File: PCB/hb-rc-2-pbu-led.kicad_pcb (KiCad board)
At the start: 2 copper layers, 49.5 x 45 mm, 33 parts, among them IC1 CC1101, J1 WS2812B LED 3V3 Lvl, J10 3V3 PAD, J11 5V PAD, J12 DIN, J13 DOUT, J14 VCC, J15 VCC, J16 GND, J4 WS2812B LED 5V Lvl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

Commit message: pcb update
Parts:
- D1: value LED -> D1
- SW2: value BTN1 -> SW2
- SW3: value BTN2 -> SW3
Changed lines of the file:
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@@
-(kicad_pcb (version 20171130) (host pcbnew "(5.1.4-0-10_14)")
+(kicad_pcb (version 20171130) (host pcbnew "(5.1.4)-1")
   (general
     (thickness 1.6)
@@
       (effects (font (size 1 1) (thickness 0.15)))
     )
-    (fp_text value BTN1 (at 2.667 -1.8415 90) (layer F.SilkS)
+    (fp_text value SW2 (at 2.667 -1.8415 90) (layer F.SilkS)
       (effects (font (size 1 1) (thickness 0.15)))
     )
@@
       (effects (font (size 1 1) (thickness 0.15)))
     )
-    (fp_text value BTN2 (at 2.794 -1.8415 270) (layer F.SilkS)
+    (fp_text value SW3 (at 2.794 -1.8415 270) (layer F.SilkS)
       (effects (font (size 1 1) (thickness 0.15)))
     )
@@
       (effects (font (size 1 1) (thickness 0.15)))
     )
-    (fp_text value LED (at 2.54 2.96 90) (layer F.SilkS)
+    (fp_text value D1 (at 2.54 2.96 90) (layer F.SilkS)
       (effects (font (size 1 1) (thickness 0.15)))
     )
@@
     (connect_pads (clearance 0.508))
     (min_thickness 0.254)
-    (fill (arc_segments 32) (thermal_gap 0.508) (thermal_bridge_width 0.508))
+    (fill yes (arc_segments 32) (thermal_gap 0.508) (thermal_bridge_width 0.508))
     (polygon
       (pts
@@
     (connect_pads (clearance 0.508))
     (min_thickness 0.254)
-    (fill (arc_segments 32) (thermal_gap 0.508) (thermal_bridge_width 0.508))
+    (fill yes (arc_segments 32) (thermal_gap 0.508) (thermal_bridge_width 0.508))
     (polygon
       (pts

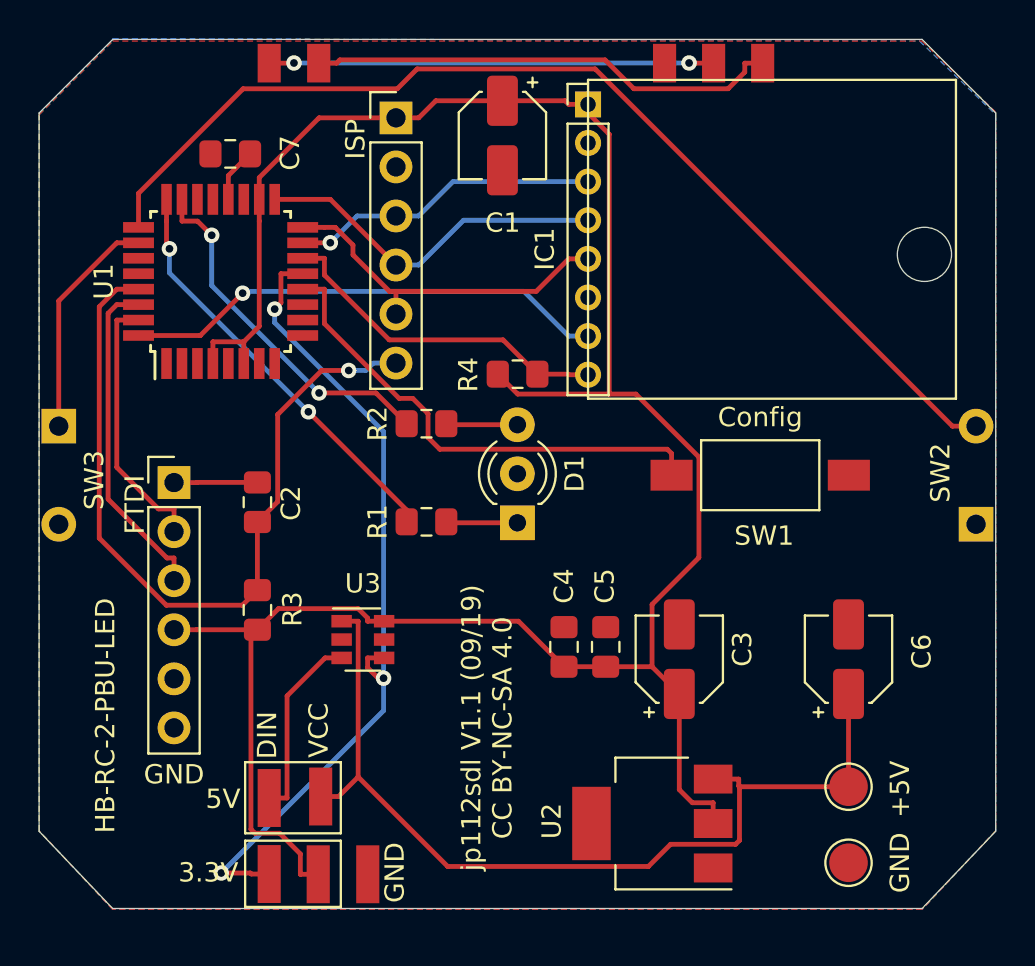
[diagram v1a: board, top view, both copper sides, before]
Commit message: fixed wrong ws2812b pin order
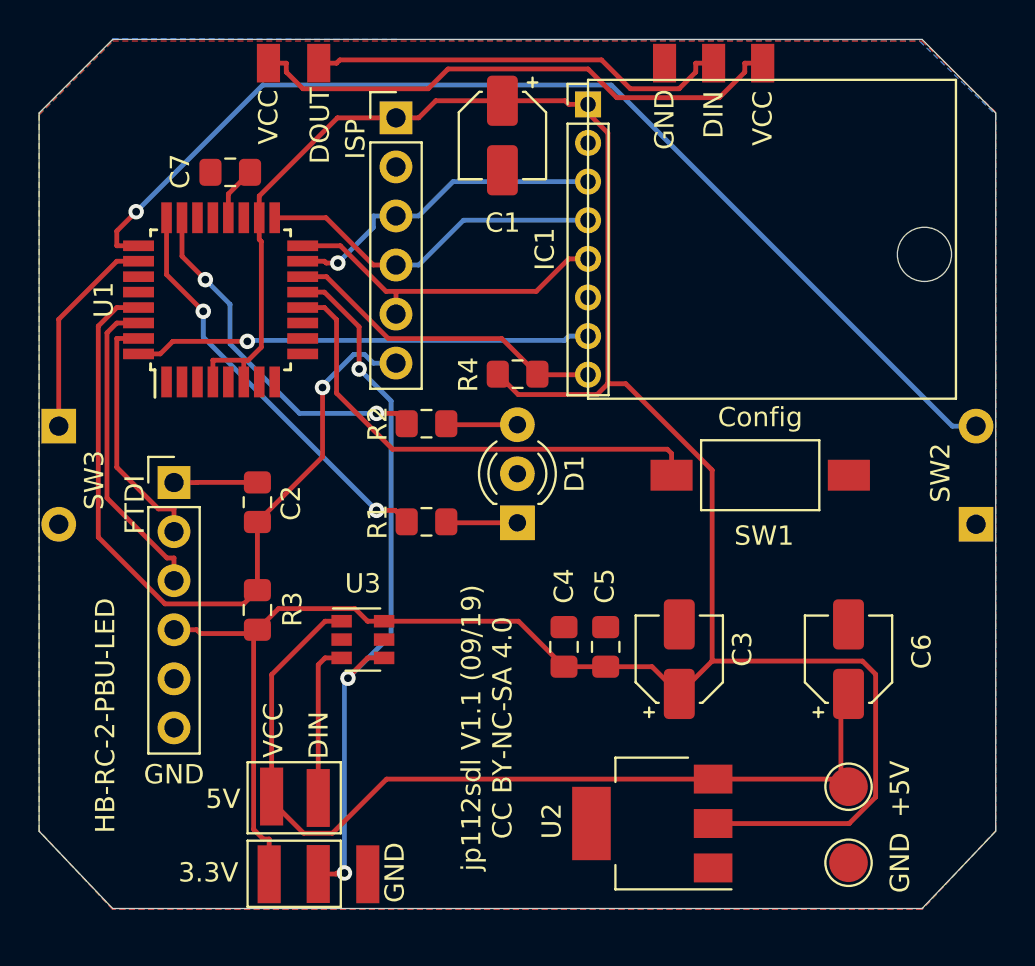
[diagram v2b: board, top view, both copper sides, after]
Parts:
- moved J14 2.60 mm to (89.3, 54.2)
- moved J13 2.56 mm to (91.9, 54.2)
- moved J1 2.54 mm to (91.9, 96.2)
- moved J10 2.54 mm to (89.4, 96.2)
- moved J4 2.54 mm to (91.9, 92.3)
- moved J11 2.54 mm to (89.5, 92.2)
- moved C7 0.95 mm to (87.4, 59.9)
- moved U1 0.95 mm to (86.9, 66.5)
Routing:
- net +3V3: track 123.1 -> 138.7 mm
- net /WS_LED: track 43.0 -> 37.3 mm
- net Net-(J14-Pad1): track 24.5 -> 28.5 mm
- net Net-(J4-Pad1): track 9.85 -> 8.26 mm
- net Net-(IC1-Pad7): track 25.2 -> 23.7 mm
- net Net-(SW2-Pad2): track 55.5 -> 56.8 mm, vias 0 -> 1
- net /RESET: track 41.1 -> 40.0 mm
- net Net-(J12-Pad1): track 23.0 -> 22.0 mm, vias 2 -> 0
- net Net-(SW3-Pad1): track 11.9 -> 10.9 mm
- net /TX: track 13.8 -> 12.8 mm
- net /RX: track 17.2 -> 16.3 mm
- net Net-(IC1-Pad8): track 17.8 -> 16.9 mm
- net /MOSI: track 16.1 -> 16.9 mm
- net /MISO: track 18.3 -> 17.6 mm
- net +5V: track 48.5 -> 47.8 mm

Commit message: fixed missing GND connections
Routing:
- net GND: track 0.00 -> 6.26 mm, vias 0 -> 5
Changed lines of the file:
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@@
     (thickness 1.6)
     (drawings 35)
-    (tracks 209)
+    (tracks 220)
     (zones 0)
     (modules 33)
@@
   (gr_line (start 127 56.81) (end 127 94) (layer Edge.Cuts) (width 0.05))
   (gr_line (start 81.28 53) (end 123.19 53) (layer Edge.Cuts) (width 0.05))
+  (segment (start 86.468 60.0065) (end 86.342 59.8805) (width 0.25) (layer F.Cu) (net 1))
+  (segment (start 86.468 62.2345) (end 86.468 60.0065) (width 0.25) (layer F.Cu) (net 1))
+  (segment (start 87.268 70.7345) (end 87.268 72.8155) (width 0.25) (layer F.Cu) (net 1))
+  (segment (start 85.668 70.7345) (end 85.668 72.5105) (width 0.25) (layer F.Cu) (net 1))
+  (segment (start 87.268 72.8155) (end 87.268 72.8155) (width 0.25) (layer F.Cu) (net 1))
+  (via (at 87.268 72.8155) (size 0.8) (drill 0.4) (layers F.Cu B.Cu) (net 1))
+  (segment (start 85.668 72.5105) (end 85.668 72.5105) (width 0.25) (layer F.Cu) (net 1))
+  (via (at 85.668 72.5105) (size 0.8) (drill 0.4) (layers F.Cu B.Cu) (net 1))
+  (via (at 108.204 54.0385) (size 0.8) (drill 0.4) (layers F.Cu B.Cu) (net 1))
+  (via (at 123.317 58.166) (size 0.8) (drill 0.4) (layers F.Cu B.Cu) (net 1))
+  (via (at 116.3955 66.04) (size 0.8) (drill 0.4) (layers F.Cu B.Cu) (net 1))
   (segment (start 95.9485 57.0611) (end 97.1238 57.0611) (width 0.25) (layer F.Cu) (net 2))
   (segment (start 101.46 56.1755) (end 98.0094 56.1755) (width 0.25) (layer F.Cu) (net 2))

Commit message: fex missing GND connections
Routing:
- net GND: track 6.26 -> 12.0 mm, vias 5 -> 8
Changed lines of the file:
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@@
-(kicad_pcb (version 20171130) (host pcbnew "(5.1.4-0-10_14)")
+(kicad_pcb (version 20171130) (host pcbnew "(5.1.4)-1")
   (general
     (thickness 1.6)
     (drawings 35)
-    (tracks 220)
+    (tracks 228)
     (zones 0)
     (modules 33)
@@
   (via (at 123.317 58.166) (size 0.8) (drill 0.4) (layers F.Cu B.Cu) (net 1))
   (via (at 116.3955 66.04) (size 0.8) (drill 0.4) (layers F.Cu B.Cu) (net 1))
+  (via (at 106.1085 76.3016) (size 0.8) (drill 0.4) (layers F.Cu B.Cu) (net 1))
+  (via (at 90.7542 86.1441) (size 0.8) (drill 0.4) (layers F.Cu B.Cu) (net 1))
+  (segment (start 91.154199 85.744101) (end 90.7542 86.1441) (width 0.25) (layer F.Cu) (net 1))
+  (segment (start 91.154199 85.273801) (end 91.154199 85.744101) (width 0.25) (layer F.Cu) (net 1))
+  (segment (start 92.354 84.074) (end 91.154199 85.273801) (width 0.25) (layer F.Cu) (net 1))
+  (segment (start 93.134 84.074) (end 92.354 84.074) (width 0.25) (layer F.Cu) (net 1))
+  (segment (start 93.134 84.074) (end 95.334 84.074) (width 0.25) (layer F.Cu) (net 1))
+  (via (at 89.9541 57.8993) (size 0.8) (drill 0.4) (layers F.Cu B.Cu) (net 1))
   (segment (start 95.9485 57.0611) (end 97.1238 57.0611) (width 0.25) (layer F.Cu) (net 2))
   (segment (start 101.46 56.1755) (end 98.0094 56.1755) (width 0.25) (layer F.Cu) (net 2))
